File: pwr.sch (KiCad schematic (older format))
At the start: 63 parts, among them SW1 KMR231NGLFS, U1 FT601, U10 MIC94310, U11 PAM2305, U4 ECP5, U6 PAM2305, U7 NCP186, U8 MIC94310, U9 MIC94310, X2 JTAG

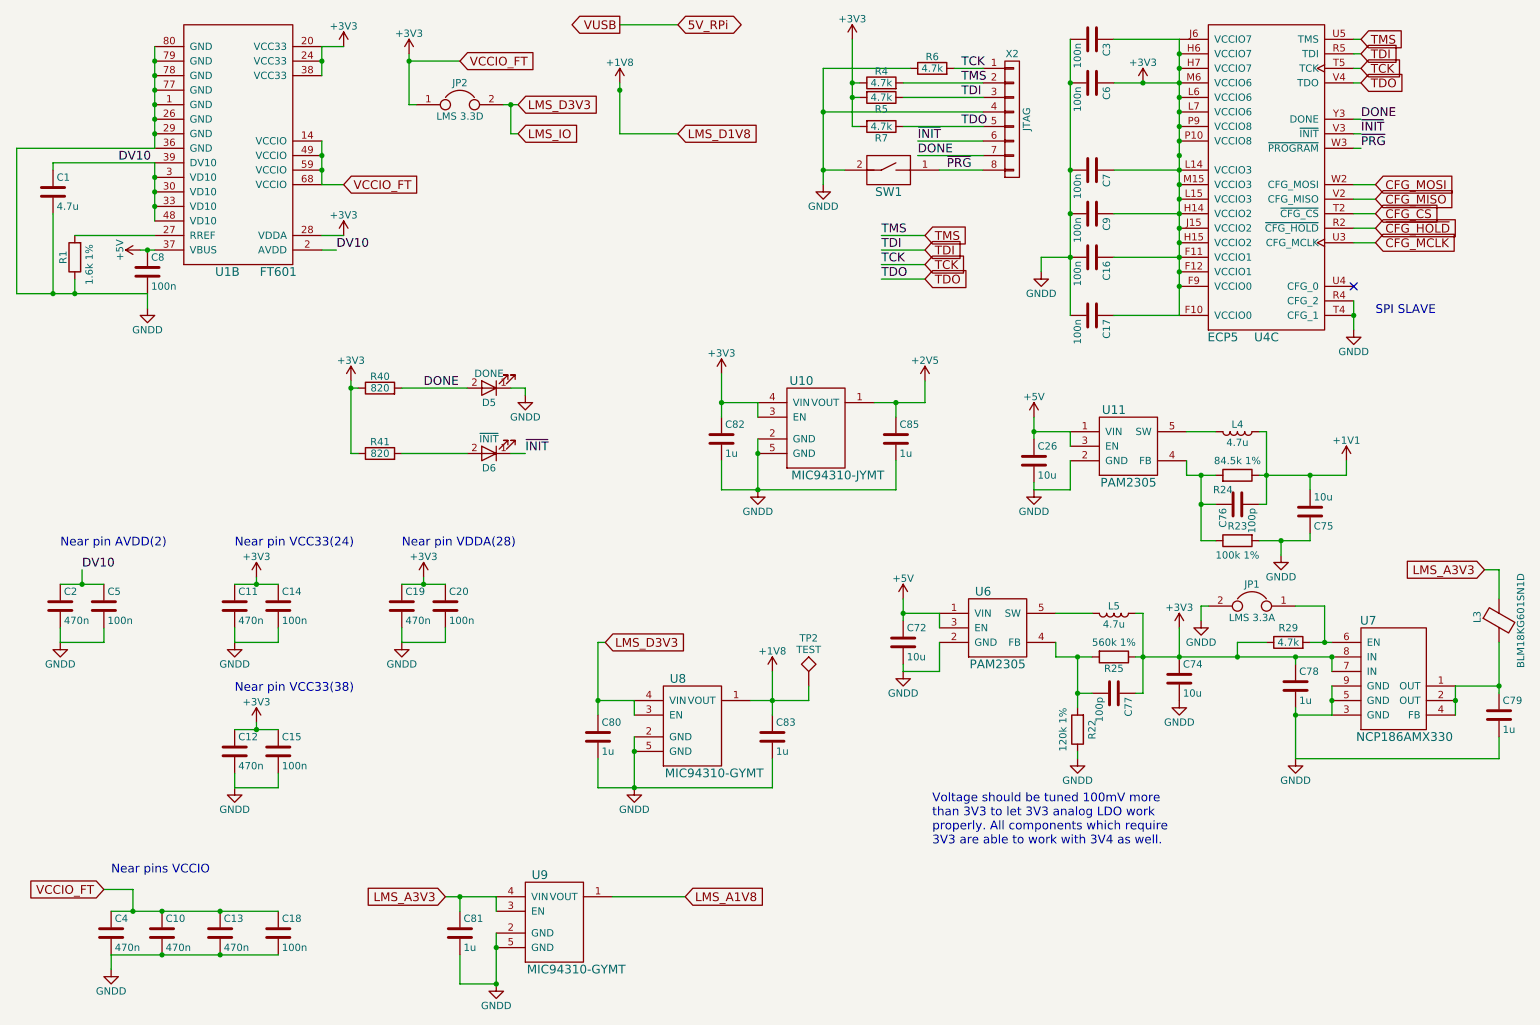
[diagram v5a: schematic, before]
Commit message: Prepared BOM and changed some part numbers for unpopular ones. Added manufacture PN for each part.
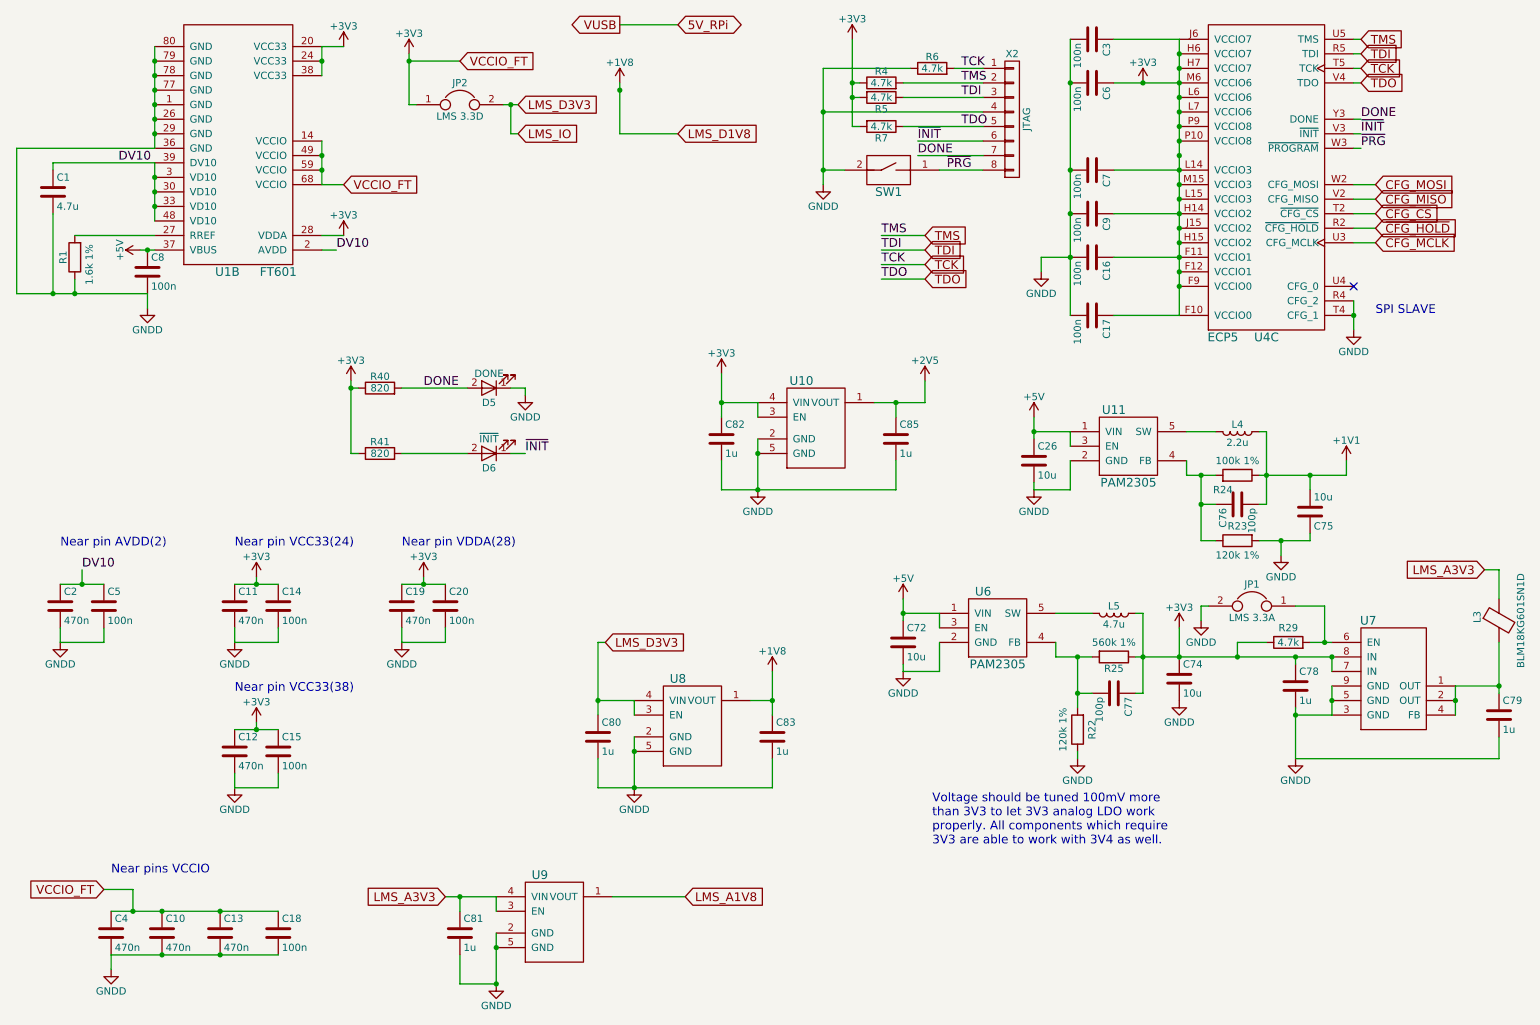
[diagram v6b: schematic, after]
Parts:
- removed TP2: TEST, Measurement_Points:Measurement_Point_Square-SMD-Pad_Small, symbol TEST
- C1: manf# (none) -> CC0603KRX5R6BB475
- C2: manf# (none) -> CC0603KRX7R7BB474
- C26: manf# (none) -> C2012X5R1C106K085AC
- C3: manf# (none) -> CC0603KRX7R7BB104
- C76: manf# (none) -> 0603YC101KAT2A
- D5: manf# (none) -> LTST-C190GKT
- D6: manf# (none) -> LTST-C190EKT
- JP1: manf# (none) -> 0022288200
- L4: value 4.7u -> 2.2u; footprint Inductors:Inductor_Taiyo-Yuden_MD-4040 -> Inductors_SMD:Inductor_Taiyo-Yuden_MD-4040; Part SRN4018-4R7M -> (none); manf# (none) -> LQH3NPN2R2MMEL
- L5: footprint Inductors:Inductor_Taiyo-Yuden_MD-4040 -> Inductors_SMD:Inductor_Taiyo-Yuden_MD-4040; Part SRN4018-4R7M -> (none); manf# (none) -> ASPI-4030S-4R7M-T
- R1: manf# (none) -> RC0603FR-071K6L
- R22: manf# (none) -> RC0603FR-07120KL
- R23: value 100k 1% -> 120k 1%; manf# (none) -> RC0603FR-07120KL
- R24: value 84.5k 1% -> 100k 1%; manf# (none) -> RC0603FR-07100KL
- R25: manf# (none) -> RC0603FR-07560KL
- R29: manf# (none) -> RC0603JR-074K7L
- SW1: manf# (none) -> KMR231NGLFS
- U1: manf# (none) -> FT601Q-B-T
- U10: Part MIC94310-JYMT -> (none); manf# (none) -> MIC94310-JYMT
- U11, U6: manf# (none) -> PAM2305DABADJ
- U4: manf# (none) -> LFE5U-25F-6BG381I
- U7: Part NCP186AMX330 -> (none); manf# (none) -> NCP186AMX330
- U8, U9: Part MIC94310-GYMT -> (none); manf# (none) -> MIC94310-GYMT
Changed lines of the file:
@@
 LIBS:valves
 LIBS:sdr
-LIBS:usb-type-c
 LIBS:sdr-cache
 EELAYER 25 0
@@
 F 2 "sdr-foots:QFN_76" H 2200 6300 60  0001 C CNN
 F 3 "" H 2200 6300 60  0001 C CNN
+F 4 "FT601Q-B-T" H 1800 2500 60  0001 C CNN "manf#"
 	2    1800 2500
 	1    0    0    -1
@@
 F 2 "Resistors_SMD:R_0603" V 980 2450 50  0001 C CNN
 F 3 "" H 1050 2450 50  0000 C CNN
+F 4 "RC0603FR-071K6L" H 1050 2450 60  0001 C CNN "manf#"
 	1    1050 2450
 	-1   0    0    1
@@
 F 2 "Capacitors_SMD:C_0603" H 938 1850 50  0001 C CNN
 F 3 "" H 900 2000 50  0000 C CNN
+F 4 "CC0603KRX5R6BB475" H 900 2000 60  0001 C CNN "manf#"
 	1    900  2000
 	1    0    0    -1
@@
 F 2 "Capacitors_SMD:C_0603" H 988 4700 50  0001 C CNN
 F 3 "" H 950 4850 50  0000 C CNN
+F 4 "CC0603KRX7R7BB474" H 950 4850 60  0001 C CNN "manf#"
 	1    950  4850
 	1    0    0    -1
@@
 F 2 "sdr-foots:ECP5_381" H 7300 3500 60  0001 C CNN
 F 3 "" H 7300 3500 60  0001 C CNN
+F 4 "LFE5U-25F-6BG381I" H 8850 2950 60  0001 C CNN "manf#"
 	3    8850 2950
 	1    0    0    -1
@@
 P 9050 3650
 F 0 "L4" V 9000 3650 50  0000 C CNN
-F 1 "4.7u" V 9125 3650 50  0000 C CNN
-F 2 "Inductors:Inductor_Taiyo-Yuden_MD-4040" H 9050 3650 50  0001 C CNN
+F 1 "2.2u" V 9125 3650 50  0000 C CNN
+F 2 "Inductors_SMD:Inductor_Taiyo-Yuden_MD-4040" H 9050 3650 50  0001 C CNN
 F 3 "" H 9050 3650 50  0000 C CNN
-F 4 "SRN4018-4R7M" V 9050 3650 60  0001 C CNN "Part"
+F 4 "LQH3NPN2R2MMEL" H 9050 3650 60  0001 C CNN "manf#"
 	1    9050 3650
 	0    -1   1    0
@@
 F 0 "L5" V 8150 4900 50  0000 C CNN
 F 1 "4.7u" V 8275 4900 50  0000 C CNN
-F 2 "Inductors:Inductor_Taiyo-Yuden_MD-4040" H 8200 4900 50  0001 C CNN
+F 2 "Inductors_SMD:Inductor_Taiyo-Yuden_MD-4040" H 8200 4900 50  0001 C CNN
 F 3 "" H 8200 4900 50  0000 C CNN
-F 4 "SRN4018-4R7M" V 8200 4900 60  0001 C CNN "Part"
+F 4 "ASPI-4030S-4R7M-T" H 8200 4900 60  0001 C CNN "manf#"
 	1    8200 4900
 	0    1    1    0
@@
 P 9050 3950
 F 0 "R24" V 8950 3850 50  0000 C CNN
-F 1 "84.5k 1%" V 9150 3950 50  0000 C CNN
+F 1 "100k 1%" V 9150 3950 50  0000 C CNN
 F 2 "Resistors_SMD:R_0603" V 8980 3950 50  0001 C CNN
 F 3 "" H 9050 3950 50  0000 C CNN
+F 4 "RC0603FR-07100KL" H 9050 3950 60  0001 C CNN "manf#"
 	1    9050 3950
 	0    1    -1   0
@@
 P 9050 4400
 F 0 "R23" V 8950 4400 50  0000 C CNN
-F 1 "100k 1%" V 9150 4400 50  0000 C CNN
+F 1 "120k 1%" V 9150 4400 50  0000 C CNN
 F 2 "Resistors_SMD:R_0603" V 8980 4400 50  0001 C CNN
 F 3 "" H 9050 4400 50  0000 C CNN
+F 4 "RC0603FR-07120KL" H 9050 4400 60  0001 C CNN "manf#"
 	1    9050 4400
 	0    -1   1    0
@@
 F 2 "Capacitors_SMD:C_0603" H 9088 4000 50  0001 C CNN
 F 3 "" H 9050 4150 50  0000 C CNN
+F 4 "0603YC101KAT2A" H 9050 4150 60  0001 C CNN "manf#"
 	1    9050 4150
 	0    -1   1    0
@@
 F 2 "Resistors_SMD:R_0603" V 8130 5200 50  0001 C CNN
 F 3 "" H 8200 5200 50  0000 C CNN
+F 4 "RC0603FR-07560KL" H 8200 5200 60  0001 C CNN "manf#"
 	1    8200 5200
 	0    1    1    0
@@
 F 2 "Resistors_SMD:R_0603" V 7880 5700 50  0001 C CNN
 F 3 "" H 7950 5700 50  0000 C CNN
+F 4 "RC0603FR-07120KL" H 7950 5700 60  0001 C CNN "manf#"
 	1    7950 5700
 	-1   0    0    1
@@
 F 2 "sdr-foots:DFN-8-1EP_1.6x1.2mm_Pitch0.4mm" H 8750 6250 60  0001 C CNN
 F 3 "" H 8750 6250 60  0001 C CNN
-F 4 "NCP186AMX330" H 10200 5650 60  0000 C CNN "Part"
+F 4 "NCP186AMX330" H 9900 5700 60  0001 C CNN "manf#"
 	1    9900 5700
 	1    0    0    -1
@@
 F 2 "sdr-foots:DFN-4" H 4550 5800 60  0001 C CNN
 F 3 "" H 4550 5800 60  0001 C CNN
-F 4 "MIC94310-GYMT" H 5450 5900 60  0000 C CNN "Part"
+F 4 "MIC94310-GYMT" H 5100 5950 60  0001 C CNN "manf#"
 	1    5100 5950
 	1    0    0    -1
@@
 F 2 "sdr-foots:DFN-4" H 3600 7150 60  0001 C CNN
 F 3 "" H 3600 7150 60  0001 C CNN
-F 4 "MIC94310-GYMT" H 4500 7250 60  0000 C CNN "Part"
+F 4 "MIC94310-GYMT" H 4150 7300 60  0001 C CNN "manf#"
 	1    4150 7300
 	1    0    0    -1
@@
 F 2 "sdr-foots:DFN-4" H 5400 3750 60  0001 C CNN
 F 3 "" H 5400 3750 60  0001 C CNN
-F 4 "MIC94310-JYMT" H 6300 3850 60  0000 C CNN "Part"
+F 4 "MIC94310-JYMT" H 5950 3900 60  0001 C CNN "manf#"
 	1    5950 3900
 	1    0    0    -1
@@
 F 2 "Capacitors_SMD:C_0603" H 8088 800 50  0001 C CNN
 F 3 "" H 8050 950 50  0000 C CNN
+F 4 "CC0603KRX7R7BB104" H 8050 950 60  0001 C CNN "manf#"
 	1    8050 950
 	0    1    1    0
@@
 F 2 "TO_SOT_Packages_SMD:SOT-23-5" H 6850 4950 60  0001 C CNN
 F 3 "" H 6850 4950 60  0001 C CNN
+F 4 "PAM2305DABADJ" H 7200 5200 60  0001 C CNN "manf#"
 	1    7200 5200
 	1    0    0    -1
@@
 F 2 "TO_SOT_Packages_SMD:SOT-23-5" H 7750 3700 60  0001 C CNN
 F 3 "" H 7750 3700 60  0001 C CNN
+F 4 "PAM2305DABADJ" H 8100 3950 60  0001 C CNN "manf#"
 	1    8100 3950
 	1    0    0    -1
@@
 F 2 "Capacitors_SMD:C_0805" H 7688 3700 50  0001 C CNN
 F 3 "" H 7650 3850 50  0000 C CNN
+F 4 "C2012X5R1C106K085AC" H 7650 3850 60  0001 C CNN "manf#"
 	1    7650 3850
 	1    0    0    -1
@@
 F 2 "Pin_Headers:Pin_Header_Angled_1x02_Pitch2.54mm" H 9150 4850 50  0001 C CNN
 F 3 "" H 9150 4850 50  0001 C CNN
+F 4 "0022288200" H 9150 4850 60  0001 C CNN "manf#"
 	1    9150 4850
 	-1   0    0    -1
@@
 F 2 "Resistors_SMD:R_0603" V 9330 5100 50  0001 C CNN
 F 3 "" H 9400 5100 50  0001 C CNN
+F 4 "RC0603JR-074K7L" H 9400 5100 60  0001 C CNN "manf#"
 	1    9400 5100
 	0    -1   -1   0
@@
 F 3 "" H 3700 1400 50  0001 C CNN
 	1    3700 1400
-	1    0    0    -1
-$EndComp
-$Comp
-L TEST TP2
-U 1 1 5933AA96
-P 6100 5400
-F 0 "TP2" H 6100 5700 50  0000 C BNN
-F 1 "TEST" H 6100 5650 50  0000 C CNN
-F 2 "Measurement_Points:Measurement_Point_Square-SMD-Pad_Small" H 6100 5400 50  0001 C CNN
-F 3 "" H 6100 5400 50  0001 C CNN
-	1    6100 5400
 	1    0    0    -1
 $EndComp
@@
 F 2 "LEDs:LED_0603" H 3900 3350 50  0001 C CNN
 F 3 "" H 3900 3350 50  0001 C CNN
+F 4 "LTST-C190GKT" H 3900 3350 60  0001 C CNN "manf#"
 	1    3900 3350
 	-1   0    0    1
@@
 F 2 "LEDs:LED_0603" H 3900 3800 50  0001 C CNN
 F 3 "" H 3900 3800 50  0001 C CNN
+F 4 "LTST-C190EKT" H 3900 3800 60  0001 C CNN "manf#"
 	1    3900 3800
 	-1   0    0    1
@@
 F 2 "sdr-foots:Switch_KMR2" H 7300 1750 60  0001 C CNN
 F 3 "" H 7300 1750 60  0001 C CNN
-F 4 "~PROGRAM" H 6650 1950 60  0001 C CNN "Name"
+F 4 "KMR231NGLFS" H 6650 1950 60  0001 C CNN "manf#"
+F 5 "~PROGRAM" H 6650 1950 60  0001 C CNN "Name"
 	1    6650 1950
 	-1   0    0    -1
@@
 	5850 5300 5850 5600
 Wire Wire Line
-	5700 5500 6100 5500
+	5700 5500 5850 5500
 Wire Wire Line
 	4650 5100 4650 5600
@@
 Connection ~ 4050 1400
 Wire Wire Line
-	6100 5500 6100 5400
-Wire Wire Line
 	9550 5100 9700 5100

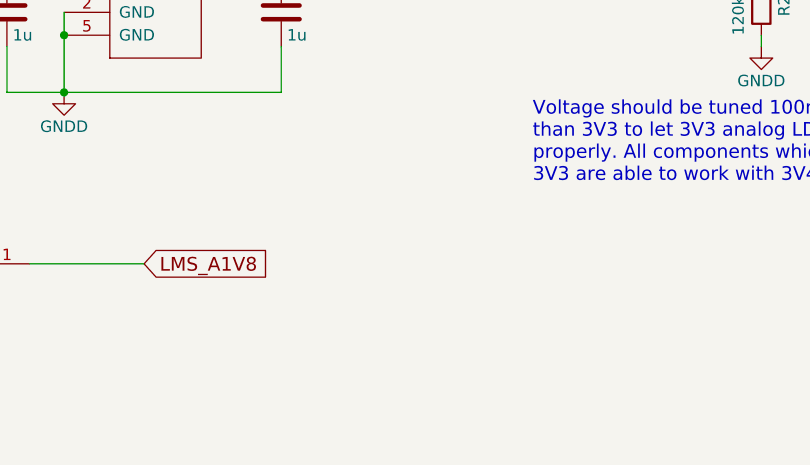
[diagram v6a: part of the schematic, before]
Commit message: Add logo, rev. GND testpoints etc in silkscreen.
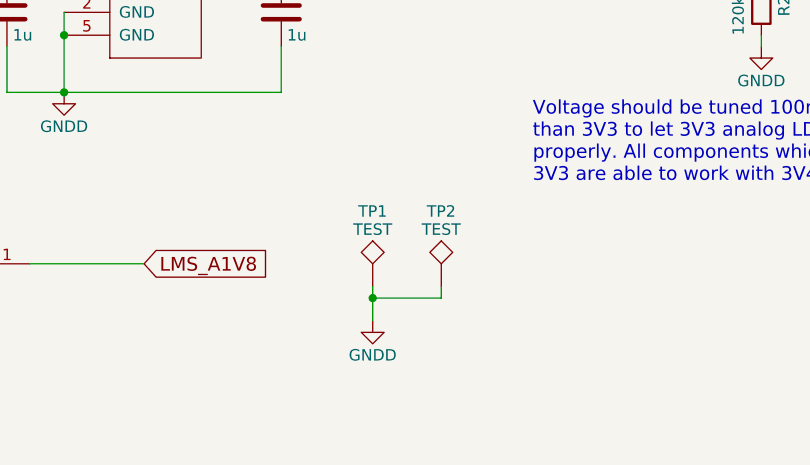
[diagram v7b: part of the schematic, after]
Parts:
- added TP1, TP2: TEST, Measurement_Points:Test_Point_Keystone_5015_Micro-Minature, symbol TEST
- JP1: manf# 0022288200 -> M20-9960245
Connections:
- net GNDD: now also TP1.1, TP2.1

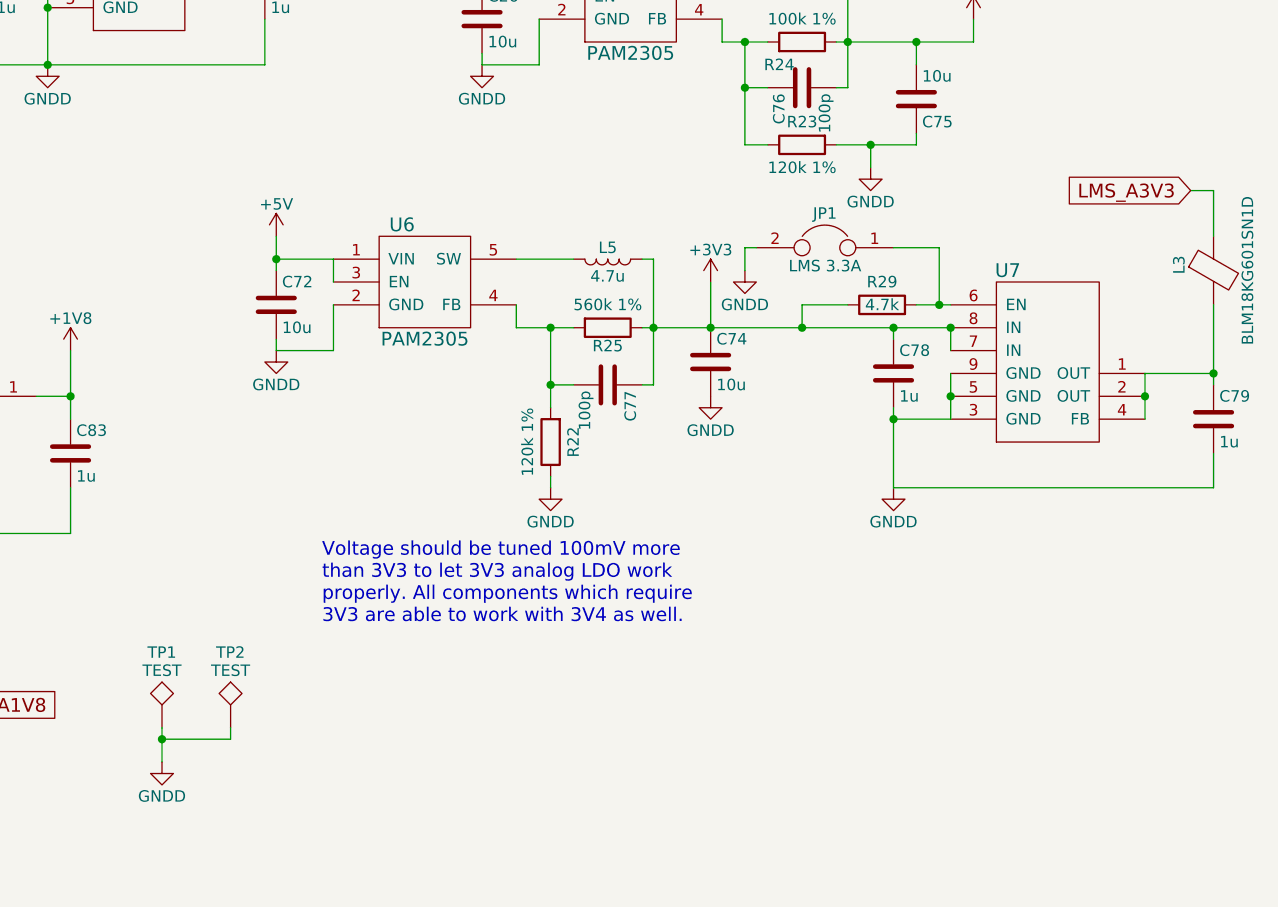
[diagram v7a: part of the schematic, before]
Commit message: Finish fixing problems: 1. LDO 3V3A has been changed as well as it CAPs 2. Silkscreen fixed 3. Mask expansion is changed
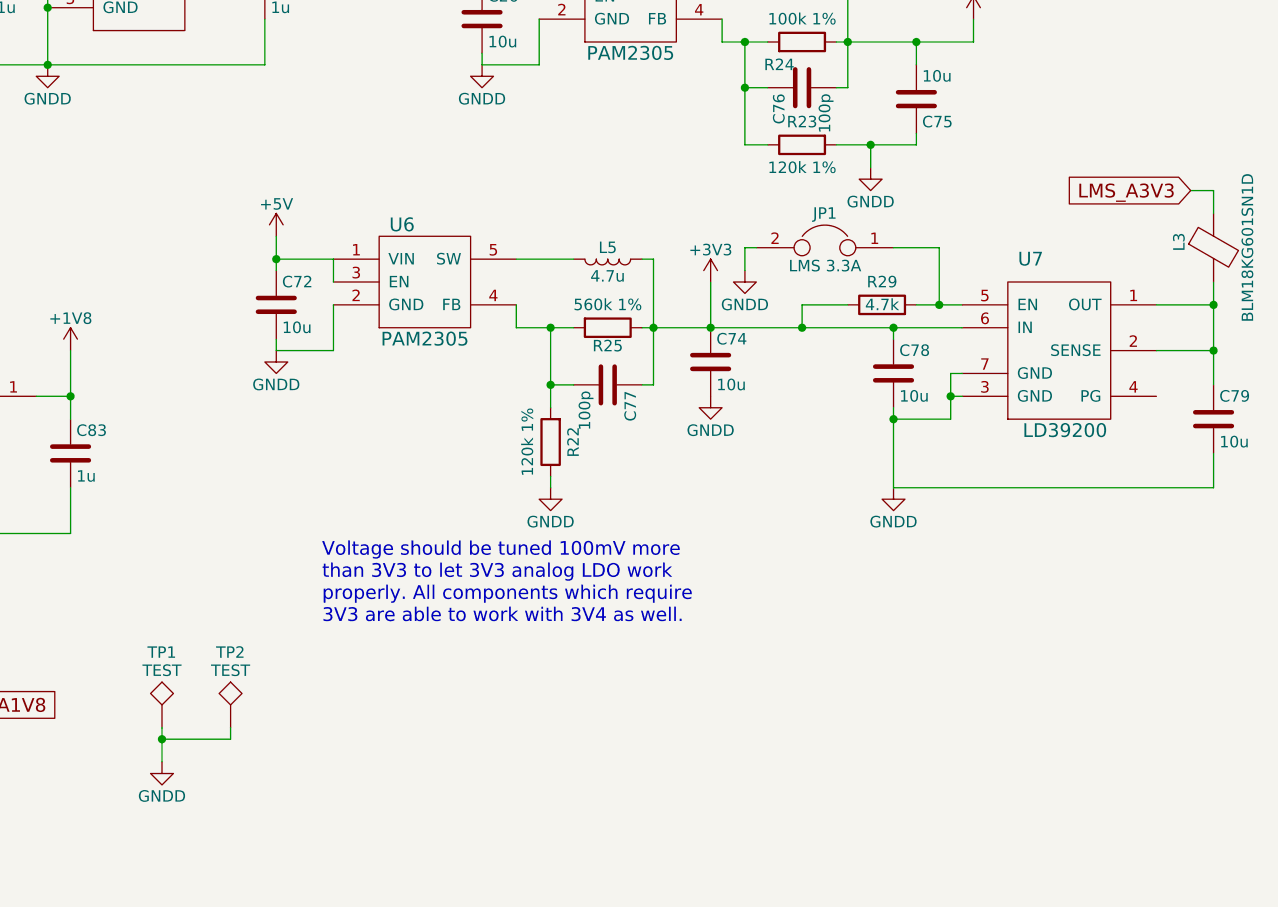
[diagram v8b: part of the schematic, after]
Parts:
- removed U7: NCP186, sdr-foots:DFN-8-1EP_1.6x1.2mm_Pitch0.4mm, symbol NCP186
- added U7: LD39200, Housings_DFN_QFN:DFN-6-1EP_3x3mm_Pitch0.95mm, symbol LD39200
- C78, C79: value 1u -> 10u; footprint Capacitors_SMD:C_0603 -> Capacitors_SMD:C_0805
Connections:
- net +3V3: now also U7.6 (IN)
- net GNDD: now also U7.3 (GND), U7.7 (GND)
- net at C79.1, L3.2: now also U7.1 (OUT), U7.2 (SENSE)
- net at JP1.1, R29.2: now also U7.5 (EN)
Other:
- moved on the sheet: L3
